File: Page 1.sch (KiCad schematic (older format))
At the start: 18 parts, among them P1 CONN HEADER SMD 6POS 2.54MM, U1 ATmega328P-AU, U801 MCP7940N-xSN, Y801 32.7680 kHz

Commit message: Updates
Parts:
- removed LED1: BLUE LED, symbol Device:LED
- removed R10, R11: R10K0, symbol Device:R
- removed R12: 470k, symbol Device:R
- added C102: 0.12uF, Capacitor_SMD:C_0805_2012Metric_Pad1.15x1.40mm_HandSolder, symbol Device:C
- added C103, C104: 0.1uF, Capacitor_SMD:C_0603_1608Metric_Pad1.05x0.95mm_HandSolder, symbol Device:C
- added C105, C106: 18pF, Capacitor_SMD:C_0603_1608Metric_Pad1.05x0.95mm_HandSolder, symbol Device:C
- added Y101: 16.00 MHz, Name Plate Class Project:Oscillator_ABM3-16.000MHZ-B2-T, symbol Name~Plate~Class~Library:Oscillator_ABM3-16.000MHZ-B2-T
- B801: footprint (none) -> Name Plate Class Project:BAT_BK-883
- C101: renamed from C104; footprint (none) -> Capacitor_SMD:C_0603_1608Metric_Pad1.05x0.95mm_HandSolder
- R101: renamed from R2; footprint (none) -> Resistor_SMD:R_0603_1608Metric_Pad1.05x0.95mm_HandSolder
- R102: renamed from R3; footprint (none) -> Resistor_SMD:R_0603_1608Metric_Pad1.05x0.95mm_HandSolder
- R103: renamed from R1; footprint (none) -> Resistor_SMD:R_0603_1608Metric_Pad1.05x0.95mm_HandSolder
- U801: footprint (none) -> Package_SO:SOIC-8_3.9x4.9mm_P1.27mm
- renumbered P1 to J101
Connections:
- net labels added: LED_IND, MEGA_nRST
- net labels removed: D8_LED, MEGA_RST#
- wire segments 98 -> 128
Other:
- moved on the sheet: C101, J101, R101, R102, R103, U1

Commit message: Updates
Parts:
- removed B801: BK-883, Name Plate Class Project:BAT_BK-883, symbol Name~Plate~Class~Library:BK-883
- removed C801: 0.1uF, Capacitor_SMD:C_0603_1608Metric_Pad1.05x0.95mm_HandSolder, symbol Device:C
- removed C802, C803: 10pF, Capacitor_SMD:C_0603_1608Metric_Pad1.05x0.95mm_HandSolder, symbol Device:C
- removed R801: 10k0, Resistor_SMD:R_0603_1608Metric_Pad1.05x0.95mm_HandSolder, symbol Device:R
- removed U801: MCP7940N-xSN, Package_SO:SOIC-8_3.9x4.9mm_P1.27mm, symbol Timer:MCP7940N-xSN
- removed Y801: 32.7680 kHz, Name Plate Class Project:Oscillator_MC-405_32.7680K-D__ROHS, symbol Name~Plate~Class~Library:Oscillator_MC-405_32.7680K-D__ROHS
- J101: footprint (none) -> Name Plate Class Project:Molex_PinHeader_2x03
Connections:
- wire segments 128 -> 99
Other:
- note removed: "Real Time Clock"
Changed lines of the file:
@@
 $Descr A4 11693 8268
 encoding utf-8
-Sheet 2 4
+Sheet 2 10
 Title ""
 Date ""
@@
 F 0 "J101" H 2650 6200 50  0000 R TNN
 F 1 "CONN HEADER SMD 6POS 2.54MM" H 2650 6300 50  0000 R TNN
-F 2 "" H 2500 5950 50  0001 C CNN
-F 3 "~" H 2500 5950 50  0001 C CNN
+F 2 "Name Plate Class Project:Molex_PinHeader_2x03" H 2500 5950 50  0001 C CNN
+F 3 "https://www.molex.com/pdm_docs/sd/713085404_sd.pdf" H 2500 5950 50  0001 C CNN
 	1    2500 5950
 	-1   0    0    1
@@
 	1650 6050 1650 5700
 $Comp
-L Timer:MCP7940N-xSN U801
-U 1 1 5EACC70E
-P 8900 5700
-F 0 "U801" H 9150 5300 50  0000 C CNN
-F 1 "MCP7940N-xSN" H 9350 5200 50  0000 C CNN
-F 2 "Package_SO:SOIC-8_3.9x4.9mm_P1.27mm" H 8900 5700 50  0001 C CNN
-F 3 "http://ww1.microchip.com/downloads/en/DeviceDoc/20005010F.pdf" H 8900 5700 50  0001 C CNN
-	1    8900 5700
-	1    0    0    -1
-$EndComp
-$Comp
 L Name~Plate~Class~Library:LCD_ER-TFTM024-3 LCD1
 U 1 1 5EAD1968
@@
 	1    0    0    -1
 $EndComp
-$Comp
-L Device:C C802
-U 1 1 5EB14F87
-P 10150 5400
-F 0 "C802" V 10000 5400 50  0000 C CNN
-F 1 "10pF" V 10300 5400 50  0000 C CNN
-F 2 "Capacitor_SMD:C_0603_1608Metric_Pad1.05x0.95mm_HandSolder" H 10188 5250 50  0001 C CNN
-F 3 "~" H 10150 5400 50  0001 C CNN
-	1    10150 5400
-	0    1    1    0
-$EndComp
-$Comp
-L Device:C C803
-U 1 1 5EB166B0
-P 10150 6000
-F 0 "C803" V 10000 6000 50  0000 C CNN
-F 1 "10pF" V 10300 6000 50  0000 C CNN
-F 2 "Capacitor_SMD:C_0603_1608Metric_Pad1.05x0.95mm_HandSolder" H 10188 5850 50  0001 C CNN
-F 3 "~" H 10150 6000 50  0001 C CNN
-	1    10150 6000
-	0    1    1    0
-$EndComp
-$Comp
-L Name~Plate~Class~Library:Oscillator_MC-405_32.7680K-D__ROHS Y801
-U 1 1 5EB20688
-P 9650 5700
-F 0 "Y801" H 9550 5550 50  0000 L CNN
-F 1 "32.7680 kHz" H 9400 5850 50  0000 L CNN
-F 2 "Name Plate Class Project:Oscillator_MC-405_32.7680K-D__ROHS" H 9550 5400 50  0001 L BNN
-F 3 "https://support.epson.biz/td/api/doc_check.php?dl=brief_MC-405&lang=en" H 9550 5300 50  0001 L BNN
-	1    9650 5700
-	0    1    1    0
-$EndComp
-Wire Wire Line
-	9300 5800 9350 5800
-Wire Wire Line
-	9350 5800 9350 6000
-Wire Wire Line
-	9350 6000 9650 6000
-Wire Wire Line
-	10300 6000 10400 6000
-Connection ~ 9650 6000
-Wire Wire Line
-	9650 6000 10000 6000
-Wire Wire Line
-	9300 5600 9350 5600
-Wire Wire Line
-	9350 5600 9350 5400
-Wire Wire Line
-	9350 5400 9650 5400
-Wire Wire Line
-	10300 5400 10400 5400
-Connection ~ 9650 5400
-Wire Wire Line
-	9650 5400 10000 5400
-$Comp
-L power:GND #PWR0112
-U 1 1 5EB2D987
-P 10400 5400
-F 0 "#PWR0112" H 10400 5150 50  0001 C CNN
-F 1 "GND" V 10405 5272 50  0000 R CNN
-F 2 "" H 10400 5400 50  0001 C CNN
-F 3 "" H 10400 5400 50  0001 C CNN
-	1    10400 5400
-	0    -1   -1   0
-$EndComp
-$Comp
-L power:GND #PWR0113
-U 1 1 5EB2E8ED
-P 10400 6000
-F 0 "#PWR0113" H 10400 5750 50  0001 C CNN
-F 1 "GND" V 10405 5872 50  0000 R CNN
-F 2 "" H 10400 6000 50  0001 C CNN
-F 3 "" H 10400 6000 50  0001 C CNN
-	1    10400 6000
-	0    -1   -1   0
-$EndComp
-$Comp
-L Name~Plate~Class~Library:BK-883 B801
-U 1 1 5EAD0B5B
-P 7850 5150
-F 0 "B801" H 7850 4883 50  0000 C CNN
-F 1 "BK-883" H 7850 4974 50  0000 C CNN
-F 2 "Name Plate Class Project:BAT_BK-883" H 7700 5400 50  0001 L BNN
-F 3 "https://www.memoryprotectiondevices.com/datasheets/BK-883-datasheet.pdf" H 7700 4800 50  0001 L BNN
-F 4 "MPD" H 7700 4850 50  0001 L BNN "Field4"
-F 5 "L" H 7700 4750 50  0001 L BNN "Field5"
-	1    7850 5150
-	-1   0    0    1
-$EndComp
-Wire Wire Line
-	8500 5800 8300 5800
-Text Label 7950 5800 0    50   ~ 0
-RTC_INT
-Text Notes 8300 6500 0    98   ~ 20
-Real Time Clock
-Connection ~ 8300 5800
-Wire Wire Line
-	8300 5800 7950 5800
-$Comp
-L Device:R R801
-U 1 1 5EADC695
-P 8300 4750
-F 0 "R801" H 8370 4796 50  0000 L CNN
-F 1 "10k0" H 8370 4705 50  0000 L CNN
-F 2 "Resistor_SMD:R_0603_1608Metric_Pad1.05x0.95mm_HandSolder" V 8230 4750 50  0001 C CNN
-F 3 "~" H 8300 4750 50  0001 C CNN
-	1    8300 4750
-	1    0    0    -1
-$EndComp
-$Comp
-L Device:C C801
-U 1 1 5EAE96FD
-P 7500 4800
-F 0 "C801" H 7150 4850 50  0000 L CNN
-F 1 "0.1uF" H 7150 4750 50  0000 L CNN
-F 2 "Capacitor_SMD:C_0603_1608Metric_Pad1.05x0.95mm_HandSolder" H 7538 4650 50  0001 C CNN
-F 3 "https://www.yageo.com/upload/media/product/productsearch/datasheet/mlcc/UPY-GPHC_X7R_6.3V-to-50V_18.pdf" H 7500 4800 50  0001 C CNN
-	1    7500 4800
-	1    0    0    -1
-$EndComp
-Wire Wire Line
-	8900 6100 8900 6200
-$Comp
-L power:GND #PWR0114
-U 1 1 5EAEF0C2
-P 7500 6300
-F 0 "#PWR0114" H 7500 6050 50  0001 C CNN
-F 1 "GND" H 7505 6127 50  0000 C CNN
-F 2 "" H 7500 6300 50  0001 C CNN
-F 3 "" H 7500 6300 50  0001 C CNN
-	1    7500 6300
-	1    0    0    -1
-$EndComp
-Wire Wire Line
-	8300 4600 8300 4500
-Connection ~ 8300 4500
-Wire Wire Line
-	8150 5150 9000 5150
-Wire Wire Line
-	9000 5150 9000 5300
-Wire Wire Line
-	7550 5150 7500 5150
-Connection ~ 7500 5150
-Wire Wire Line
-	8900 5300 8900 4500
-Wire Wire Line
-	8300 4500 8900 4500
-Wire Wire Line
-	8300 4900 8300 5800
-Wire Wire Line
-	7500 4500 8300 4500
-Connection ~ 7500 4500
-Wire Wire Line
-	7500 4500 7500 4650
-$Comp
-L power:+3.3V #PWR0115
-U 1 1 5EB22892
-P 7500 4350
-F 0 "#PWR0115" H 7500 4200 50  0001 C CNN
-F 1 "+3.3V" H 7515 4523 50  0000 C CNN
-F 2 "" H 7500 4350 50  0001 C CNN
-F 3 "" H 7500 4350 50  0001 C CNN
-	1    7500 4350
-	1    0    0    -1
-$EndComp
-Wire Wire Line
-	7500 4350 7500 4500
-Wire Wire Line
-	7500 4950 7500 5150
-Wire Wire Line
-	7500 5150 7500 6200
-Wire Wire Line
-	7500 6200 8900 6200
-Connection ~ 7500 6200
-Wire Wire Line
-	7500 6200 7500 6300
-Wire Wire Line
-	8500 5500 7950 5500
-Wire Wire Line
-	8500 5600 7950 5600
-Text GLabel 7950 5600 0    50   Input ~ 0
-SDA
-Text GLabel 7950 5500 0    50   Input ~ 0
-SCL
 Wire Wire Line
 	2750 950  2750 850

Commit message: Updates
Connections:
- net labels added: SW1, SW2, SW3, SW4, SW5
- net labels removed: D3_SW1, D4_SW2, D5_SW2, D6_SW2, D7_SW2

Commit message: Updates
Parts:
- removed LCD1: LCD 2.4\" SPI ER-TFTM024-3, Name Plate Class Project:LCD_ER-TFTM024-3, symbol Name~Plate~Class~Library:LCD_ER-TFTM024-3
- J101: value CONN HEADER SMD 6POS 2.54MM -> Conn Header SMD
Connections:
- net labels added: ADDR_LED, BUZZER, LCD_FONT_nSELECT, LCD_nCS, MEGA_RX, MEGA_TX, SPI_CLK, SPI_MISO, SPI_MOSI
- net labels removed: A2_FONTCS#, A3_PIXEL_DATA_R, D10_LCD_SCn_R, D2_LCD_DC_R, D9_BUZZER1, LCD_CLK, LCD_CSn, LCD_SDI, LCD_SDO, MEGA_RXD, MEGA_TXD, MISO, MOSI, SCK
- wire segments 99 -> 84
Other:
- moved on the sheet: R101, R102, R103

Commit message: Updates
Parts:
- C101, C103, C104: Mftr Part No. (none) -> Yageo CC0603KPX7R7BB104
- C102: Mftr Part No. (none) -> AVX 08053C124KAT2A
- C105, C106: Mftr Part No. (none) -> Kemet C0603C180J5GACTU
- R103: DigiKey Part No. (none) -> 311-10KGRCT-ND; Mftr Part No. (none) -> Yageo RC0603JR-0710KL
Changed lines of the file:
@@
 F 2 "Capacitor_SMD:C_0603_1608Metric_Pad1.05x0.95mm_HandSolder" H 1888 1750 50  0001 C CNN
 F 3 "https://www.yageo.com/upload/media/product/productsearch/datasheet/mlcc/UPY-GPHC_X7R_6.3V-to-50V_18.pdf" H 1850 1900 50  0001 C CNN
+F 4 "Yageo CC0603KPX7R7BB104" H 1850 1900 50  0001 C CNN "Mftr Part No."
 	1    1850 1900
 	1    0    0    -1
@@
 F 2 "Capacitor_SMD:C_0805_2012Metric_Pad1.15x1.40mm_HandSolder" H 1538 2150 50  0001 C CNN
 F 3 "http://datasheets.avx.com/X7RDielectric.pdf" H 1500 2300 50  0001 C CNN
+F 4 "AVX 08053C124KAT2A" H 1500 2300 50  0001 C CNN "Mftr Part No."
 	1    1500 2300
 	1    0    0    -1
@@
 F 2 "Capacitor_SMD:C_0603_1608Metric_Pad1.05x0.95mm_HandSolder" H 1238 2650 50  0001 C CNN
 F 3 "https://www.yageo.com/upload/media/product/productsearch/datasheet/mlcc/UPY-GPHC_X7R_6.3V-to-50V_18.pdf" H 1200 2800 50  0001 C CNN
+F 4 "Yageo CC0603KPX7R7BB104" H 1200 2800 50  0001 C CNN "Mftr Part No."
 	1    1200 2800
 	1    0    0    -1
@@
 F 2 "Capacitor_SMD:C_0603_1608Metric_Pad1.05x0.95mm_HandSolder" H 938 3100 50  0001 C CNN
 F 3 "https://www.yageo.com/upload/media/product/productsearch/datasheet/mlcc/UPY-GPHC_X7R_6.3V-to-50V_18.pdf" H 900 3250 50  0001 C CNN
+F 4 "Yageo CC0603KPX7R7BB104" H 900 3250 50  0001 C CNN "Mftr Part No."
 	1    900  3250
 	1    0    0    -1
@@
 F 1 "R10K0" H 4920 2205 50  0000 L CNN
 F 2 "Resistor_SMD:R_0603_1608Metric_Pad1.05x0.95mm_HandSolder" V 4780 2250 50  0001 C CNN
-F 3 "~" H 4850 2250 50  0001 C CNN
+F 3 "https://www.yageo.com/upload/media/product/productsearch/datasheet/rchip/PYu-RC_Group_51_RoHS_L_10.pdf" H 4850 2250 50  0001 C CNN
+F 4 "311-10KGRCT-ND" H 4850 2250 50  0001 C CNN "DigiKey Part No."
+F 5 "Yageo RC0603JR-0710KL" H 4850 2250 50  0001 C CNN "Mftr Part No."
 	1    4850 2250
 	1    0    0    -1
@@
 F 2 "Capacitor_SMD:C_0603_1608Metric_Pad1.05x0.95mm_HandSolder" H 2938 4500 50  0001 C CNN
 F 3 "~" H 2900 4650 50  0001 C CNN
+F 4 "Kemet C0603C180J5GACTU" H 2900 4650 50  0001 C CNN "Mftr Part No."
 	1    2900 4650
 	0    1    1    0
@@
 F 2 "Capacitor_SMD:C_0603_1608Metric_Pad1.05x0.95mm_HandSolder" H 2938 4900 50  0001 C CNN
 F 3 "~" H 2900 5050 50  0001 C CNN
+F 4 "Kemet C0603C180J5GACTU" H 2900 5050 50  0001 C CNN "Mftr Part No."
 	1    2900 5050
 	0    1    1    0

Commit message: Updates
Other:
- note added: "ATMega Microcontroller"
- moved on the sheet: C101, C102, C103, C104, C105, C106, J101, R101, R102, R103, U1

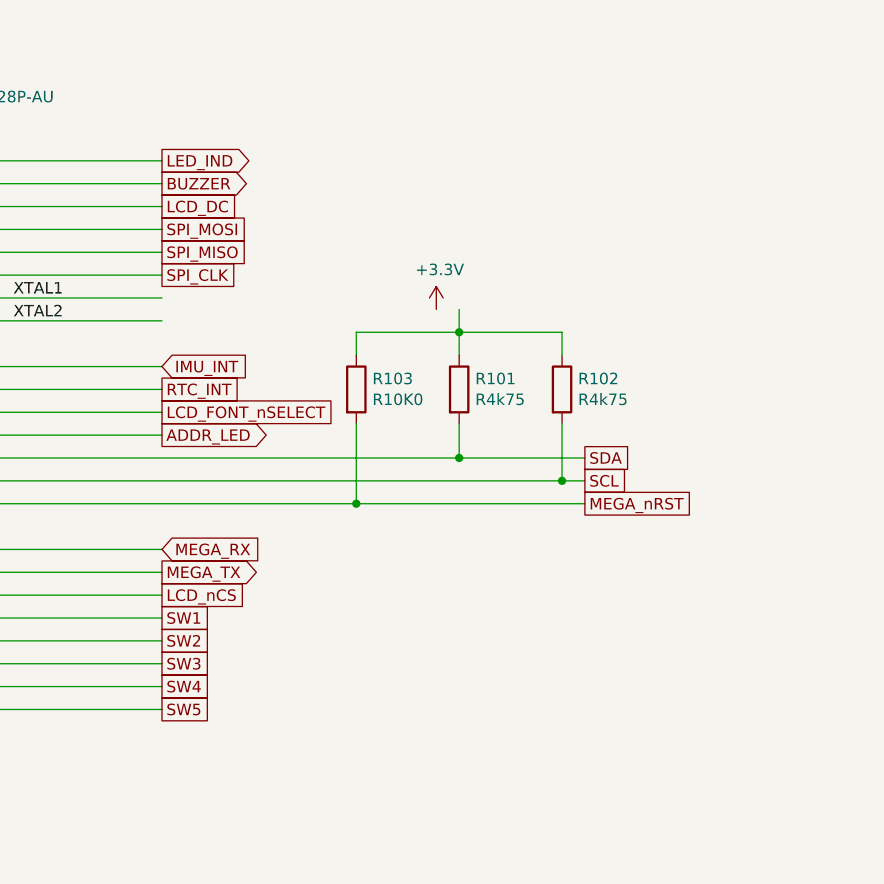
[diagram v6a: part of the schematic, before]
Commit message: Switched to Hierarchical
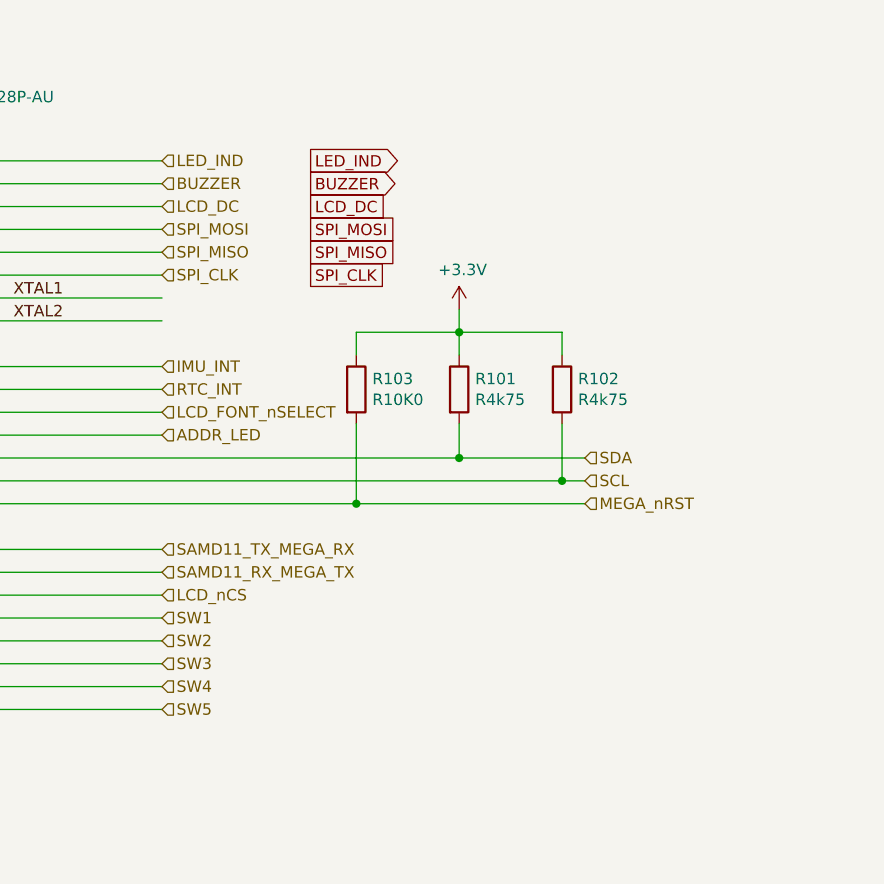
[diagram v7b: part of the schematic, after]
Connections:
- net labels added: SAMD11_RX_MEGA_TX, SAMD11_TX_MEGA_RX
- net labels removed: MEGA_RX, MEGA_TX
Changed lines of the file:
@@
 Wire Wire Line
 	4000 2450 4750 2450
-Text GLabel 4750 1350 2    50   Output ~ 0
+Text GLabel 5400 1350 2    50   Output ~ 0
 BUZZER
-Text GLabel 4750 2150 2    50   Input ~ 0
-IMU_INT
-Text GLabel 6600 2650 2    50   UnSpc ~ 0
-SCL
-Text GLabel 6600 2750 2    50   UnSpc ~ 0
-MEGA_nRST
-Text GLabel 4750 2950 2    50   Input ~ 0
-MEGA_RX
-Text GLabel 4750 3050 2    50   Output ~ 0
-MEGA_TX
-Text GLabel 4750 3250 2    50   UnSpc ~ 0
-SW1
-Text GLabel 4750 3350 2    50   UnSpc ~ 0
-SW2
-Text GLabel 4750 3450 2    50   UnSpc ~ 0
-SW3
-Text GLabel 4750 3550 2    50   UnSpc ~ 0
-SW4
-Text GLabel 4750 3650 2    50   UnSpc ~ 0
-SW5
-Text GLabel 6600 2550 2    50   UnSpc ~ 0
-SDA
 Text GLabel 9450 3200 2    50   BiDi ~ 0
 MEGA_nRST
@@
 L power:+3.3V #PWR06
 U 1 1 5EADA375
-P 5950 1900
-F 0 "#PWR06" H 5950 1750 50  0001 C CNN
-F 1 "+3.3V" H 5965 2073 50  0000 C CNN
-F 2 "" H 5950 1900 50  0001 C CNN
-F 3 "" H 5950 1900 50  0001 C CNN
-	1    5950 1900
+P 6050 1900
+F 0 "#PWR06" H 6050 1750 50  0001 C CNN
+F 1 "+3.3V" H 6065 2073 50  0000 C CNN
+F 2 "" H 6050 1900 50  0001 C CNN
+F 3 "" H 6050 1900 50  0001 C CNN
+	1    6050 1900
 	1    0    0    -1
 $EndComp
@@
 Wire Wire Line
 	8150 1300 8550 1300
-Text GLabel 4750 1250 2    50   Output ~ 0
+Text GLabel 5400 1250 2    50   Output ~ 0
 LED_IND
-Text GLabel 4750 2450 2    50   Output ~ 0
-ADDR_LED
-Text GLabel 4750 1450 2    50   UnSpc ~ 0
+Text GLabel 5400 1450 2    50   UnSpc ~ 0
 LCD_DC
-Text GLabel 4750 1550 2    50   UnSpc ~ 0
+Text GLabel 5400 1550 2    50   UnSpc ~ 0
 SPI_MOSI
-Text GLabel 4750 1650 2    50   UnSpc ~ 0
+Text GLabel 5400 1650 2    50   UnSpc ~ 0
 SPI_MISO
-Text GLabel 4750 1750 2    50   UnSpc ~ 0
+Text GLabel 5400 1750 2    50   UnSpc ~ 0
 SPI_CLK
-Text GLabel 4750 2250 2    50   UnSpc ~ 0
-RTC_INT
-Text GLabel 4750 2350 2    50   UnSpc ~ 0
-LCD_FONT_nSELECT
 Wire Wire Line
 	5600 2000 6050 2000
@@
 Wire Wire Line
 	4000 2650 6500 2650
-Text GLabel 4750 3150 2    50   UnSpc ~ 0
-LCD_nCS
 Text GLabel 9450 3400 2    50   UnSpc ~ 0
 SPI_MISO
@@
 Wire Wire Line
 	2600 2050 2600 3700
+Text HLabel 4750 2150 2    50   Input ~ 0
+IMU_INT
+Text HLabel 6600 2550 2    50   Input ~ 0
+SDA
+Text HLabel 6600 2650 2    50   Input ~ 0
+SCL
+Text HLabel 4750 3250 2    50   Input ~ 0
+SW1
+Text HLabel 4750 3350 2    50   Input ~ 0
+SW2
+Text HLabel 4750 3450 2    50   Input ~ 0
+SW3
+Text HLabel 4750 3550 2    50   Input ~ 0
+SW4
+Text HLabel 4750 3650 2    50   Input ~ 0
+SW5
+Text HLabel 4750 2250 2    50   Input ~ 0
+RTC_INT
+Text HLabel 6600 2750 2    50   Input ~ 0
+MEGA_nRST
+Text HLabel 4750 2950 2    50   Input ~ 0
+SAMD11_TX_MEGA_RX
+Text HLabel 4750 3050 2    50   Input ~ 0
+SAMD11_RX_MEGA_TX
+Text HLabel 4750 3150 2    50   Input ~ 0
+LCD_nCS
+Text HLabel 4750 2450 2    50   Input ~ 0
+ADDR_LED
+Text HLabel 4750 2350 2    50   Input ~ 0
+LCD_FONT_nSELECT
+Text HLabel 4750 1750 2    50   Input ~ 0
+SPI_CLK
+Text HLabel 4750 1650 2    50   Input ~ 0
+SPI_MISO
+Text HLabel 4750 1550 2    50   Input ~ 0
+SPI_MOSI
+Text HLabel 4750 1450 2    50   Input ~ 0
+LCD_DC
+Text HLabel 4750 1350 2    50   Input ~ 0
+BUZZER
+Text HLabel 4750 1250 2    50   Input ~ 0
+LED_IND
 $EndSCHEMATC

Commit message: Updating to Final Revision
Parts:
- added R104, R105: R10K0, Resistor_SMD:R_0603_1608Metric_Pad1.05x0.95mm_HandSolder, symbol Device:R
- renumbered C106 to C103, C105 to C104, C103 to C105, C104 to C106, R103 to R101, R101 to R102, R102 to R103
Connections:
- wire segments 84 -> 93
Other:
- moved on the sheet: C101, C102, C105, C106, R101, R102, R103, U1
